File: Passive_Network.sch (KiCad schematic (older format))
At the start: 150 parts, among them J18 CONN_01X03, J19 CONN_01X03, J20 CONN_01X08, SW2 SW_Rotary3x4, X1 P7002SCLRP, X2 P7002SCLRP, X3 P7002SCLRP, X4 P7002SCLRP, X5 P7002SCLRP, X6 P7002SCLRP

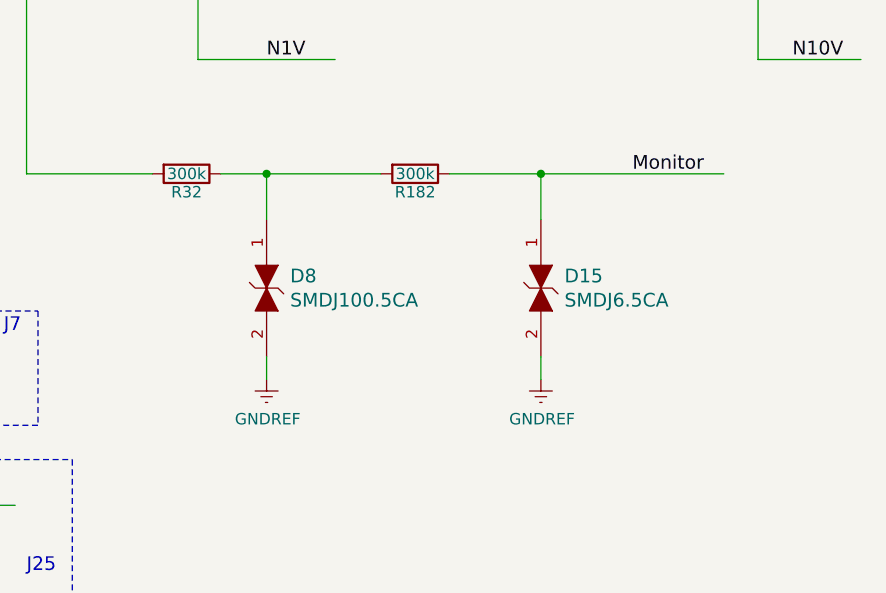
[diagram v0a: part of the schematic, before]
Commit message: 3차 PCB
1. 모니터 고압부 150k옴 2갤로 수정
2. 6.5V Zener 추가
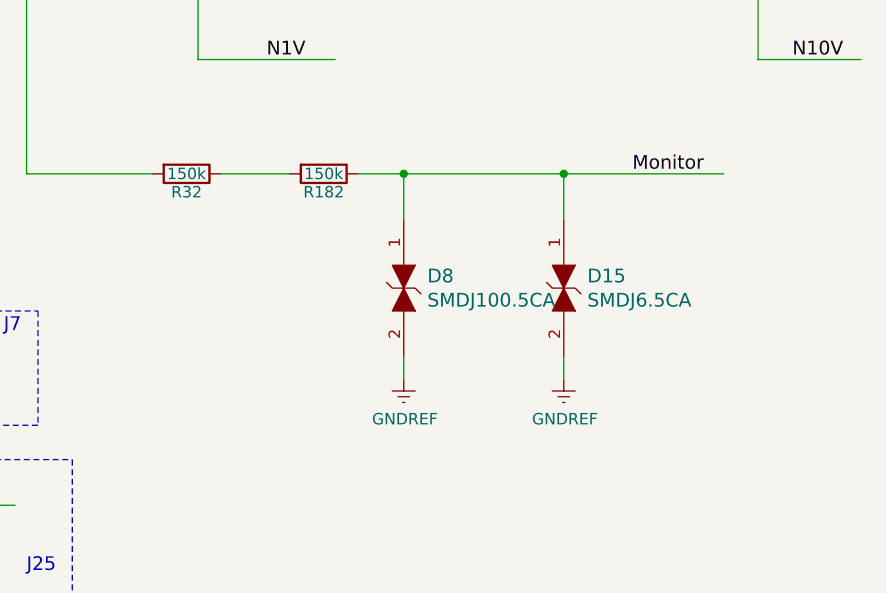
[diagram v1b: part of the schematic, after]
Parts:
- R182, R32: value 300k -> 150k
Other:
- moved on the sheet: D15, D8, R182
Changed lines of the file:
@@
 P 3900 5100
 F 0 "R32" V 3980 5100 50  0000 C CNN
-F 1 "300k" V 3900 5100 50  0000 C CNN
+F 1 "150k" V 3900 5100 50  0000 C CNN
 F 2 "Resistors_THT:R_Axial_Power_L20.0mm_W6.4mm_P22.40mm" V 3830 5100 50  0001 C CNN
 F 3 "" H 3900 5100 50  0001 C CNN
@@
 L GNDREF #PWR0113
 U 1 1 5B046D38
-P 4250 6000
-F 0 "#PWR0113" H 4250 5750 50  0001 C CNN
-F 1 "GNDREF" H 4255 5827 50  0000 C CNN
-F 2 "" H 4250 6000 50  0001 C CNN
-F 3 "" H 4250 6000 50  0001 C CNN
-	1    4250 6000
+P 4850 6000
+F 0 "#PWR0113" H 4850 5750 50  0001 C CNN
+F 1 "GNDREF" H 4855 5827 50  0000 C CNN
+F 2 "" H 4850 6000 50  0001 C CNN
+F 3 "" H 4850 6000 50  0001 C CNN
+	1    4850 6000
 	1    0    0    -1
 $EndComp
@@
 L PGB1010603MR D8
 U 1 1 5B0844BB
-P 4250 5600
-F 0 "D8" V 4197 5703 60  0000 L CNN
-F 1 "SMDJ100.5CA" V 4303 5703 60  0000 L CNN
-F 2 "Diodes_SMD:D_SMC_Handsoldering" H 4450 5800 60  0001 L CNN
-F 3 "http://www.littelfuse.com/data/en/data_sheets/littelfuse_pulseguard-esd_pgb1.pdf" H 4450 5900 60  0001 L CNN
-F 4 "F2594CT-ND" H 4450 6000 60  0001 L CNN "Digi-Key_PN"
-F 5 "PGB1010603MR" H 4450 6100 60  0001 L CNN "MPN"
-F 6 "Circuit Protection" H 4450 6200 60  0001 L CNN "Category"
-F 7 "TVS - Diodes" H 4450 6300 60  0001 L CNN "Family"
-F 8 "http://www.littelfuse.com/data/en/data_sheets/littelfuse_pulseguard-esd_pgb1.pdf" H 4450 6400 60  0001 L CNN "DK_Datasheet_Link"
-F 9 "/product-detail/en/littelfuse-inc/PGB1010603MR/F2594CT-ND/813072" H 4450 6500 60  0001 L CNN "DK_Detail_Page"
-F 10 "TVS DIODE 24VWM 150VC 0603" H 4450 6600 60  0001 L CNN "Description"
-F 11 "Littelfuse Inc." H 4450 6700 60  0001 L CNN "Manufacturer"
-F 12 "Active" H 4450 6800 60  0001 L CNN "Status"
-	1    4250 5600
+P 4850 5600
+F 0 "D8" V 4797 5703 60  0000 L CNN
+F 1 "SMDJ100.5CA" V 4903 5703 60  0000 L CNN
+F 2 "Diodes_SMD:D_SMC_Handsoldering" H 5050 5800 60  0001 L CNN
+F 3 "http://www.littelfuse.com/data/en/data_sheets/littelfuse_pulseguard-esd_pgb1.pdf" H 5050 5900 60  0001 L CNN
+F 4 "F2594CT-ND" H 5050 6000 60  0001 L CNN "Digi-Key_PN"
+F 5 "PGB1010603MR" H 5050 6100 60  0001 L CNN "MPN"
+F 6 "Circuit Protection" H 5050 6200 60  0001 L CNN "Category"
+F 7 "TVS - Diodes" H 5050 6300 60  0001 L CNN "Family"
+F 8 "http://www.littelfuse.com/data/en/data_sheets/littelfuse_pulseguard-esd_pgb1.pdf" H 5050 6400 60  0001 L CNN "DK_Datasheet_Link"
+F 9 "/product-detail/en/littelfuse-inc/PGB1010603MR/F2594CT-ND/813072" H 5050 6500 60  0001 L CNN "DK_Detail_Page"
+F 10 "TVS DIODE 24VWM 150VC 0603" H 5050 6600 60  0001 L CNN "Description"
+F 11 "Littelfuse Inc." H 5050 6700 60  0001 L CNN "Manufacturer"
+F 12 "Active" H 5050 6800 60  0001 L CNN "Status"
+	1    4850 5600
 	0    1    1    0
 $EndComp
@@
 L R R182
 U 1 1 5B33D99D
-P 4900 5100
-F 0 "R182" V 4980 5100 50  0000 C CNN
-F 1 "300k" V 4900 5100 50  0000 C CNN
-F 2 "Resistors_THT:R_Axial_Power_L20.0mm_W6.4mm_P22.40mm" V 4830 5100 50  0001 C CNN
-F 3 "" H 4900 5100 50  0001 C CNN
-	1    4900 5100
+P 4500 5100
+F 0 "R182" V 4580 5100 50  0000 C CNN
+F 1 "150k" V 4500 5100 50  0000 C CNN
+F 2 "Resistors_THT:R_Axial_Power_L20.0mm_W6.4mm_P22.40mm" V 4430 5100 50  0001 C CNN
+F 3 "" H 4500 5100 50  0001 C CNN
+	1    4500 5100
 	0    1    1    0
 $EndComp
@@
 L GNDREF #PWR01
 U 1 1 5B33D9A4
-P 5450 6000
-F 0 "#PWR01" H 5450 5750 50  0001 C CNN
-F 1 "GNDREF" H 5455 5827 50  0000 C CNN
-F 2 "" H 5450 6000 50  0001 C CNN
-F 3 "" H 5450 6000 50  0001 C CNN
-	1    5450 6000
+P 5550 6000
+F 0 "#PWR01" H 5550 5750 50  0001 C CNN
+F 1 "GNDREF" H 5555 5827 50  0000 C CNN
+F 2 "" H 5550 6000 50  0001 C CNN
+F 3 "" H 5550 6000 50  0001 C CNN
+	1    5550 6000
 	1    0    0    -1
 $EndComp
@@
 L PGB1010603MR D15
 U 1 1 5B33D9B6
-P 5450 5600
-F 0 "D15" V 5397 5703 60  0000 L CNN
-F 1 "SMDJ6.5CA" V 5503 5703 60  0000 L CNN
-F 2 "Diodes_SMD:D_SMC_Handsoldering" H 5650 5800 60  0001 L CNN
-F 3 "http://www.littelfuse.com/data/en/data_sheets/littelfuse_pulseguard-esd_pgb1.pdf" H 5650 5900 60  0001 L CNN
-F 4 "F2594CT-ND" H 5650 6000 60  0001 L CNN "Digi-Key_PN"
-F 5 "PGB1010603MR" H 5650 6100 60  0001 L CNN "MPN"
-F 6 "Circuit Protection" H 5650 6200 60  0001 L CNN "Category"
-F 7 "TVS - Diodes" H 5650 6300 60  0001 L CNN "Family"
-F 8 "http://www.littelfuse.com/data/en/data_sheets/littelfuse_pulseguard-esd_pgb1.pdf" H 5650 6400 60  0001 L CNN "DK_Datasheet_Link"
-F 9 "/product-detail/en/littelfuse-inc/PGB1010603MR/F2594CT-ND/813072" H 5650 6500 60  0001 L CNN "DK_Detail_Page"
-F 10 "TVS DIODE 24VWM 150VC 0603" H 5650 6600 60  0001 L CNN "Description"
-F 11 "Littelfuse Inc." H 5650 6700 60  0001 L CNN "Manufacturer"
-F 12 "Active" H 5650 6800 60  0001 L CNN "Status"
-	1    5450 5600
+P 5550 5600
+F 0 "D15" V 5497 5703 60  0000 L CNN
+F 1 "SMDJ6.5CA" V 5603 5703 60  0000 L CNN
+F 2 "Diodes_SMD:D_SMC_Handsoldering" H 5750 5800 60  0001 L CNN
+F 3 "http://www.littelfuse.com/data/en/data_sheets/littelfuse_pulseguard-esd_pgb1.pdf" H 5750 5900 60  0001 L CNN
+F 4 "F2594CT-ND" H 5750 6000 60  0001 L CNN "Digi-Key_PN"
+F 5 "PGB1010603MR" H 5750 6100 60  0001 L CNN "MPN"
+F 6 "Circuit Protection" H 5750 6200 60  0001 L CNN "Category"
+F 7 "TVS - Diodes" H 5750 6300 60  0001 L CNN "Family"
+F 8 "http://www.littelfuse.com/data/en/data_sheets/littelfuse_pulseguard-esd_pgb1.pdf" H 5750 6400 60  0001 L CNN "DK_Datasheet_Link"
+F 9 "/product-detail/en/littelfuse-inc/PGB1010603MR/F2594CT-ND/813072" H 5750 6500 60  0001 L CNN "DK_Detail_Page"
+F 10 "TVS DIODE 24VWM 150VC 0603" H 5750 6600 60  0001 L CNN "Description"
+F 11 "Littelfuse Inc." H 5750 6700 60  0001 L CNN "Manufacturer"
+F 12 "Active" H 5750 6800 60  0001 L CNN "Status"
+	1    5550 5600
 	0    1    1    0
 $EndComp
@@
 	3200 5100 3750 5100
 Wire Wire Line
-	5050 5100 6250 5100
-Wire Wire Line
-	4250 5900 4250 6000
-Wire Wire Line
-	4250 5300 4250 5100
-Connection ~ 4250 5100
+	4650 5100 6250 5100
+Wire Wire Line
+	4850 5900 4850 6000
 Wire Wire Line
 	9250 2550 9250 3250
@@
 Connection ~ 3850 3350
 Wire Wire Line
-	4050 5100 4750 5100
-Wire Wire Line
-	5450 5900 5450 6000
-Wire Wire Line
-	5450 5300 5450 5100
-Connection ~ 5450 5100
+	4050 5100 4350 5100
+Wire Wire Line
+	5550 5900 5550 6000
+Wire Wire Line
+	5550 5300 5550 5100
+Connection ~ 5550 5100
 Wire Wire Line
 	3450 3350 3450 3450
+Wire Wire Line
+	4850 5300 4850 5100
+Connection ~ 4850 5100
 $EndSCHEMATC

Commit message: PCB Part name
PCB Part name 수정
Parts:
- D8: value SMDJ100.5CA -> SMDJ6.5CA
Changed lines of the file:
@@
 P 4850 5600
 F 0 "D8" V 4797 5703 60  0000 L CNN
-F 1 "SMDJ100.5CA" V 4903 5703 60  0000 L CNN
+F 1 "SMDJ6.5CA" V 4903 5703 60  0000 L CNN
 F 2 "Diodes_SMD:D_SMC_Handsoldering" H 5050 5800 60  0001 L CNN
 F 3 "http://www.littelfuse.com/data/en/data_sheets/littelfuse_pulseguard-esd_pgb1.pdf" H 5050 5900 60  0001 L CNN

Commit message: 4차 PCB
U23 Wire Breakage Relay 추가
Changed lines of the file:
@@
 Connection ~ 9250 3150
 Connection ~ 9250 2900
-Connection ~ 3200 3450
 Connection ~ 3200 2450
 Wire Wire Line
